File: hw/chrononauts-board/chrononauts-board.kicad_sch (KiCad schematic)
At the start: 45 parts, among them IC1 ESP32-C3-WROOM-02-N4, IC2 TLV62568DBVR, J1 73251-1290, J2 USB4105-GF-A, U1 CC1101RGP, Y1 NX3225GA-26MHZ

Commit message: hw: generate fab outputs
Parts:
- C1, C10, C11, C12, C13, C14, C15, C16, C17, C18, C19, C2, C20, C21, C3, C4, C5, C6, C7, C8, C9: footprint ChrononautsLib:Cap_Murata_GRM_0402 -> PCBLib:Cap_Murata_GRM_0402
- C22: footprint ChrononautsLib:Cap_Murata_GRM_0603 -> PCBLib:Cap_Murata_GRM_0603
- D1, D2, D3: footprint ChrononautsLib:SODFL1006X40N -> PCBLib:SODFL1006X40N
- D4: footprint ChrononautsLib:SOD3716X135N -> PCBLib:SOD3716X135N
- IC1: footprint ChrononautsLib:ESP32C3WROOM02N4 -> PCBLib:ESP32C3WROOM02N4; symbol ChrononautsLib:ESP32-C3-WROOM-02-N4 -> PCBLib:ESP32-C3-WROOM-02-N4
- IC2: footprint ChrononautsLib:TLV62568DBVR -> PCBLib:TLV62568DBVR; symbol ChrononautsLib:TLV62568DBVR -> PCBLib:TLV62568DBVR
- J1: footprint ChrononautsLib:Molex-SD-73251-129 -> PCBLib:Molex-SD-73251-129; symbol ChrononautsLib:SD-73251-129 -> PCBLib:SD-73251-129
- J2: footprint ChrononautsLib:GCT_USB4105-GF-A -> PCBLib:GCT_USB4105-GF-A; symbol ChrononautsLib:USB4105-GF-A -> PCBLib:USB4105-GF-A
- L1, L2, L3, L4: footprint ChrononautsLib:L_Murata_LQG_0402 -> PCBLib:L_Murata_LQG_0402
- L5: footprint ChrononautsLib:ASPI0418FS -> PCBLib:ASPI0418FS
- R1: footprint ChrononautsLib:R_KOA_RK_0402 -> PCBLib:R_KOA_RK_0402
- R2, R3, R4, R5, R8: footprint ChrononautsLib:R_Vishay_CRCW_0402 -> PCBLib:R_Vishay_CRCW_0402
- R6, R7: footprint ChrononautsLib:R_Bourns_CR_0603 -> PCBLib:R_Bourns_CR_0603
- U1: footprint ChrononautsLib:CC1101RGP -> PCBLib:CC1101RGP; symbol ChrononautsLib:CC1101RGP -> PCBLib:CC1101RGP
- Y1: footprint ChrononautsLib:NX3225GA16000MSTDCRG1 -> PCBLib:NX3225GA16000MSTDCRG1; symbol ChrononautsLib:NX3225GA-26.000MHZ-EXS00A-CG01972 -> PCBLib:NX3225GA-26.000MHZ-EXS00A-CG01972

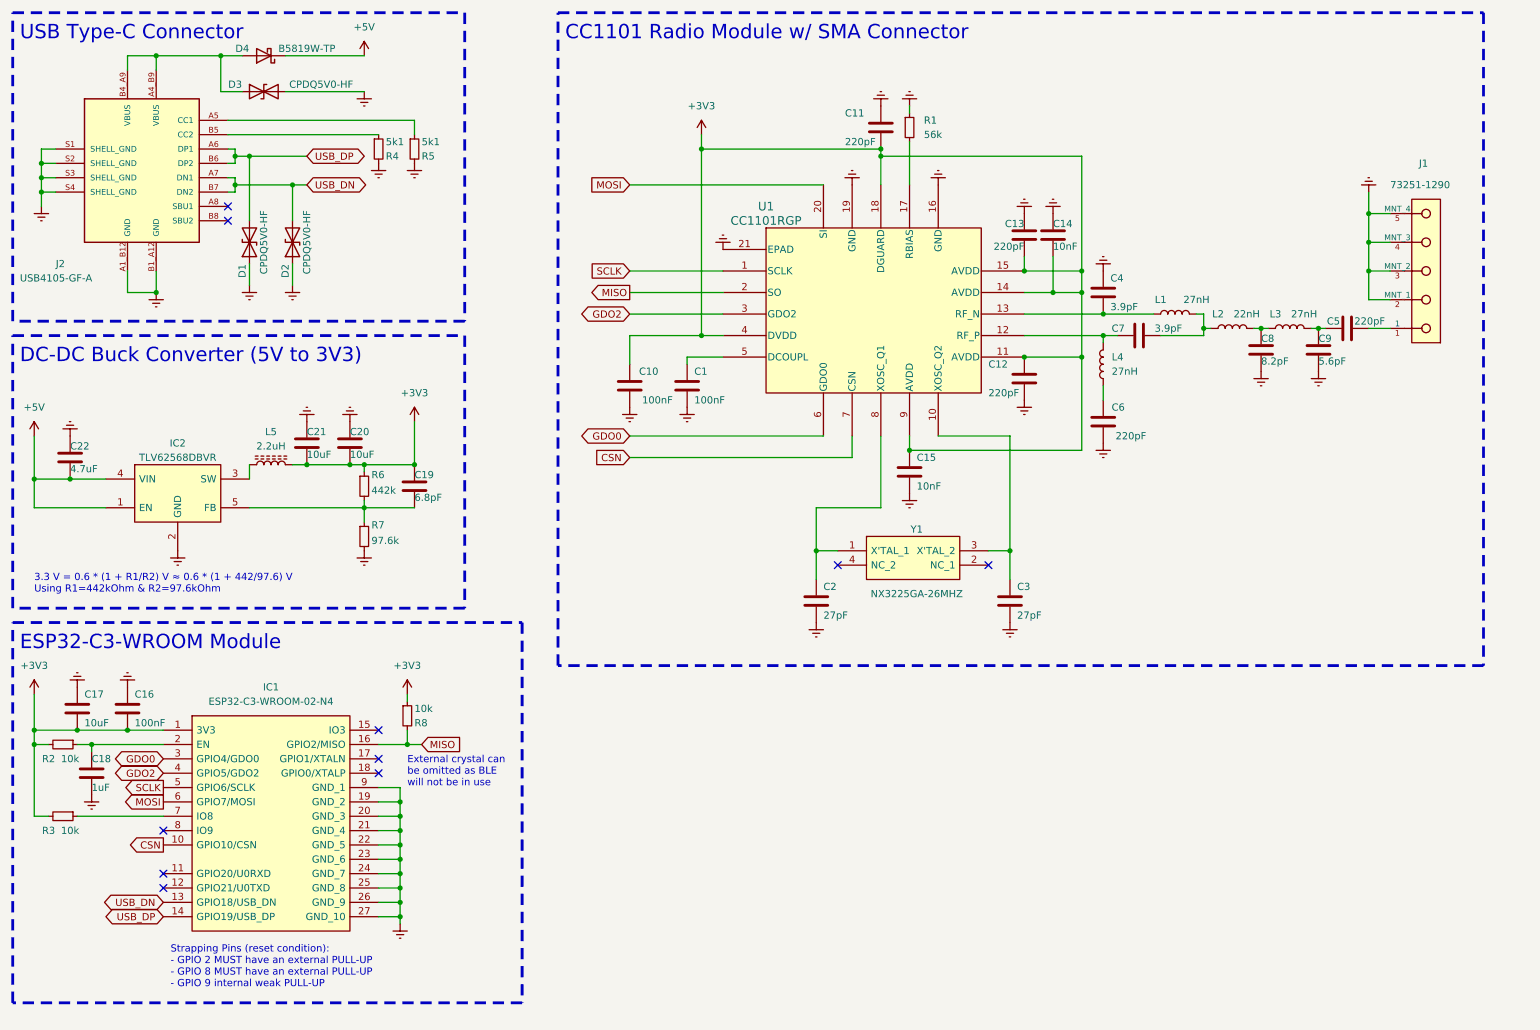
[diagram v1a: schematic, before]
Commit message: add LEDs, push button, potentiometer and I2C accelerometer (preliminary)
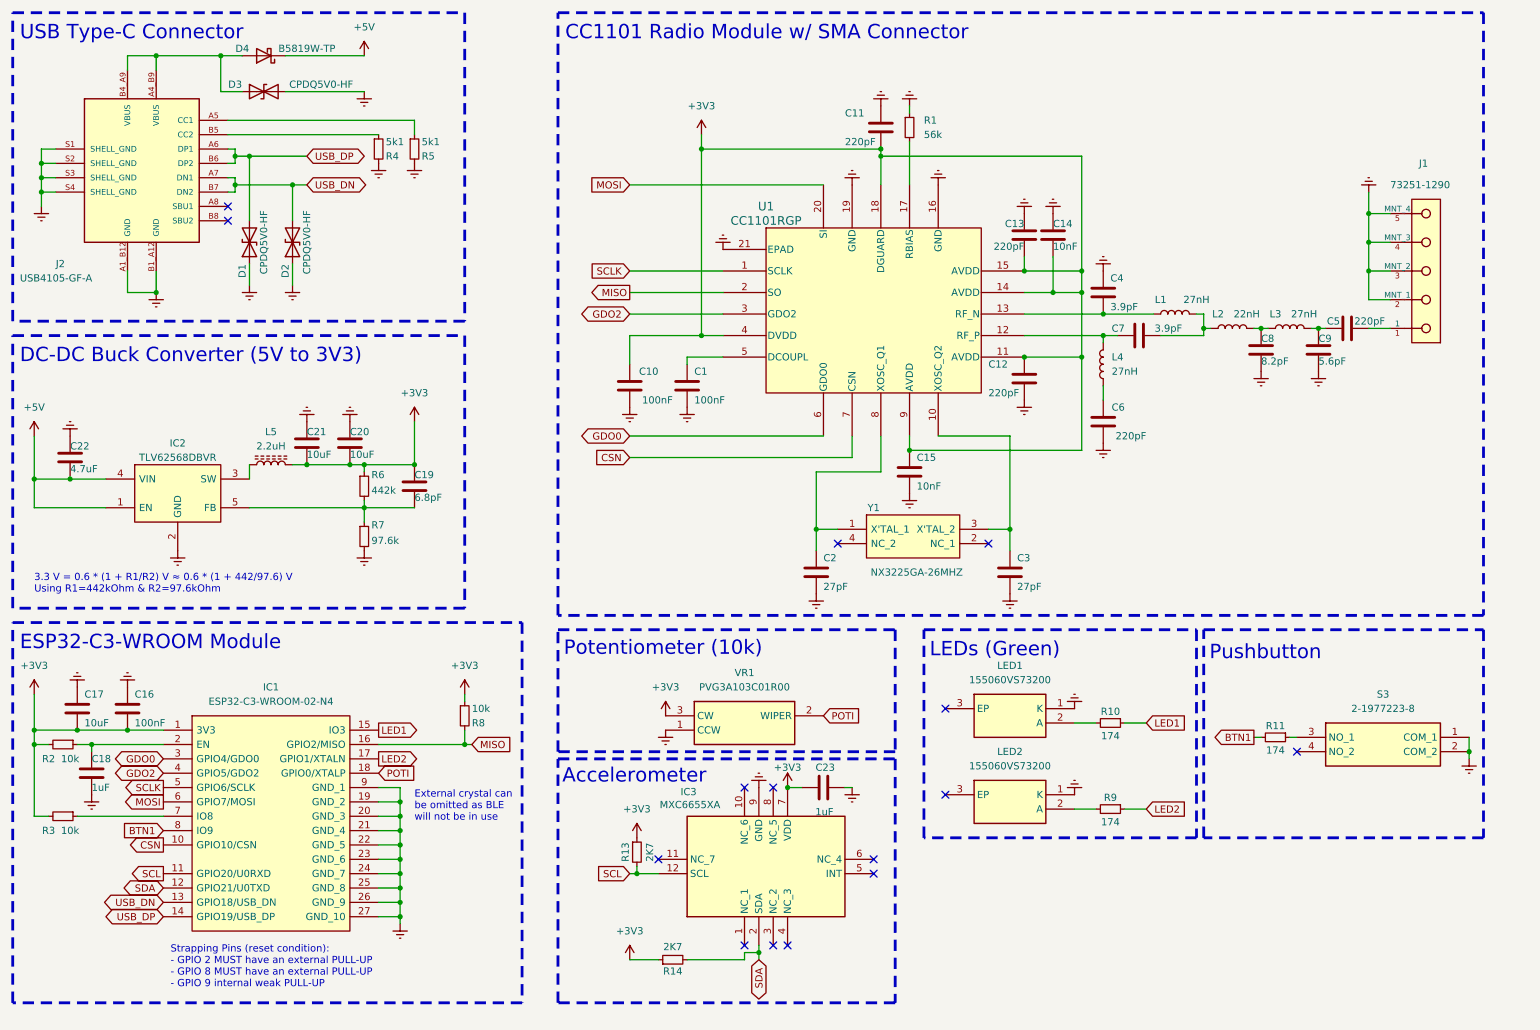
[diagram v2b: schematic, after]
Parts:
- added C23: 1uF, PCBLib:Cap_Murata_GRM_0402, symbol Device:C
- added IC3: MXC6655XA, PCBLib:MXC6655XA, symbol PCBLib:MXC6655XA
- added LED1, LED2: 155060VS73200, PCBLib:155060VS73200, symbol PCBLib:155060VS73200
- added R10, R11, R9: 174, PCBLib:R_Vishay_CRCW_0402, symbol Device:R_Small
- added R13, R14: 2K7, PCBLib:R_Vishay_CRCW_0402, symbol Device:R_Small
- added S3: 2-1977223-8, PCBLib:219772238, symbol PCBLib:2-1977223-8
- added VR1: PVG3A103C01R00, PCBLib:PVG3A103C01R00, symbol PCBLib:PVG3A103C01R00
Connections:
- net +3V3: now also C23.1, IC3.7 (VDD), R13.1, R14.1, VR1.3 (CW)
- net Earth: now also C23.2, IC3.9 (GND), LED1.1 (K), LED2.1 (K), S3.1 (COM_1), S3.2 (COM_2), VR1.1 (CCW)
- net SCL: now reaches IC1.11 (GPIO20/U0RXD)
- net SCL: now also IC3.12 (SCL), R13.2
- net SDA: now reaches IC1.12 (GPIO21/U0TXD)
- net SDA: now also IC3.2 (SDA), R14.2
- net LED1: now reaches IC1.15 (IO3)
- net LED1: now also R10.1
- net LED2: now reaches IC1.17 (GPIO1/XTALN)
- net LED2: now also R9.1
- net POTI: now reaches IC1.18 (GPIO0/XTALP)
- net POTI: now also VR1.2 (WIPER)
- net BTN1: now reaches IC1.8 (IO9)
- net BTN1: now also R11.2
- new net: LED2.2 (A), R9.2
- new net: R11.1, S3.3 (NO_1)
- new net: LED1.2 (A), R10.2
- no-connect marks 10 -> 15
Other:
- note added: "Accelerometer"
- note added: "LEDs (Green)"
- note added: "Potentiometer (10k)"
- note added: "Pushbutton"
- moved on the sheet: C2, C3, R8, Y1

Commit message: ready for production
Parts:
- added H1, H2, H4: MountingHole_Pad, MountingHole:MountingHole_2.2mm_M2_DIN965_Pad_TopBottom, symbol Mechanical:MountingHole_Pad
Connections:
- net +3V3: now also R14.2; no longer R14.1
- net SDA: now also R14.1; no longer R14.2
- net SW: now reaches IC2.3 (SW), L5.1
- no-connect marks 15 -> 18
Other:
- company: mineiwik -> chrononauts-quest
- moved on the sheet: C1, C10, C11, C12, C13, C14, C15, C19, C2, C20, C21, C22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

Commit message: generate production files
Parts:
- C1, C10, C16: LCSC (none) -> C431646
- C11, C12, C13, C5, C6: LCSC (none) -> C412611
- C14, C15: LCSC (none) -> C482489
- C17, C20, C21: LCSC (none) -> C510630
- C18, C23: LCSC (none) -> C527012
- C19: LCSC (none) -> C338054
- C2, C3: LCSC (none) -> C342944
- C22: LCSC (none) -> C77045
- C4, C7: LCSC (none) -> C565491
- C8: LCSC (none) -> C393674
- C9: LCSC (none) -> C525219
- D1, D2, D3: LCSC (none) -> C2441615
- D4: LCSC (none) -> C84354
- IC1: LCSC (none) -> C2934560
- IC2: LCSC (none) -> C163219
- IC3: LCSC (none) -> C5189050
- J2: LCSC (none) -> C3020560
- L1, L3, L4: LCSC (none) -> C12669
- L2: LCSC (none) -> C12670
- L5: LCSC (none) -> C2042636
- LED1, LED2: LCSC (none) -> C5362838
- R1: LCSC (none) -> C71703
- R10, R11, R9: LCSC (none) -> C416364
- R13, R14: LCSC (none) -> C416505
- R2, R3, R8: LCSC (none) -> C471764
- R4, R5: LCSC (none) -> C138073
- R6: LCSC (none) -> C234533
- R7: LCSC (none) -> C507495
- S3: LCSC (none) -> C2928194
- U1: LCSC (none) -> C29953
- VR1: LCSC (none) -> C840533
- Y1: LCSC (none) -> C485372

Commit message: HW: Update assembly and production data
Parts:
- S3: LCSC C2928194 -> (none)
- U1: LCSC C29953 -> (none)
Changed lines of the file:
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@@
 			)
 		)
-		(property "LCSC" "C29953"
-			(at 171.45 63.5 0)
-			(effects
-				(font
-					(size 1.27 1.27)
-				)
-				(hide yes)
-			)
-		)
 		(pin "1"
 		)
@@
 				(hide yes)
 			)
-		)
-		(property "LCSC" "C2928194"
-			(at 245.11 135.89 0)
-			(effects
-				(font
-					(size 1.27 1.27)
-				)
-				(hide yes)
-			)
